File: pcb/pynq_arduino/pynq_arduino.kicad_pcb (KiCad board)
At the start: 4 copper layers, 48.5 x 52 mm, 3 parts, among them J1 Conn_02x11_Odd_Even, J2 Conn_01x15_Pin

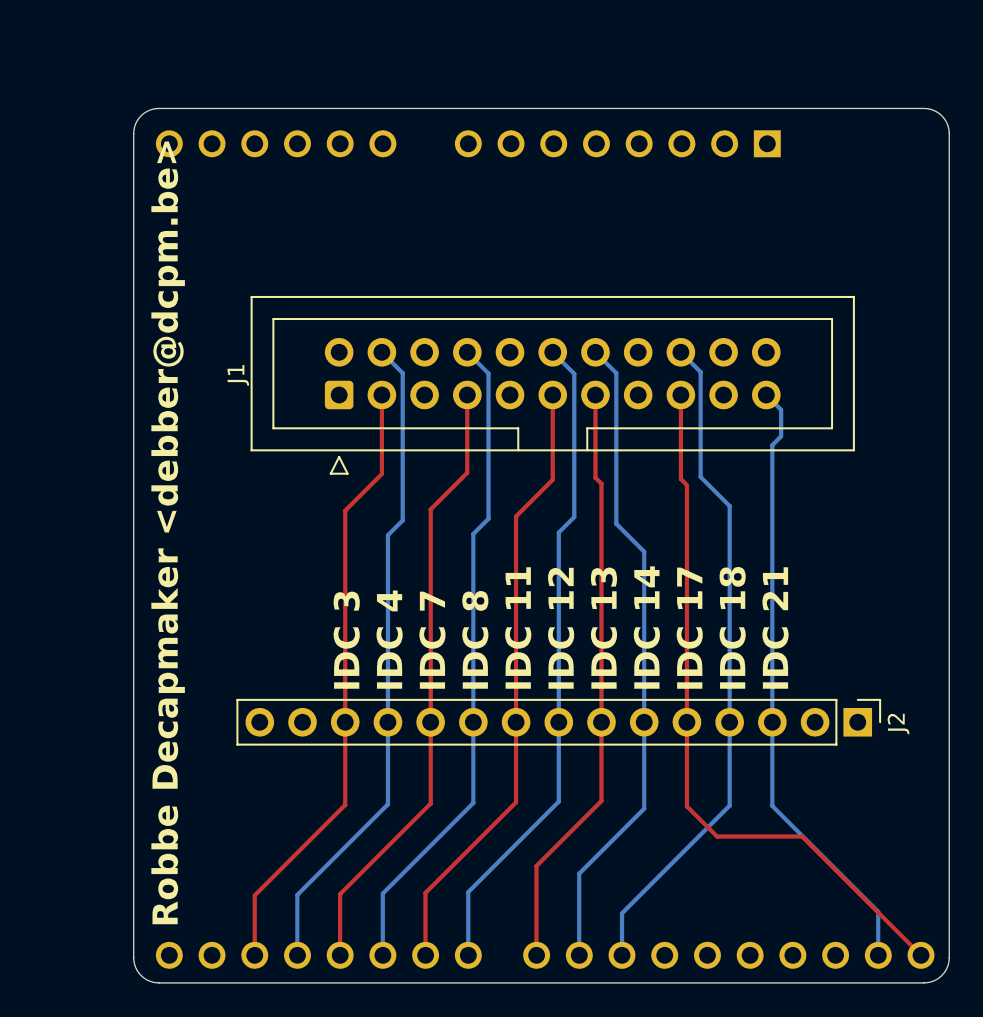
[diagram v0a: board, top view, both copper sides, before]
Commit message: Updating pynq pcb to have level shifters
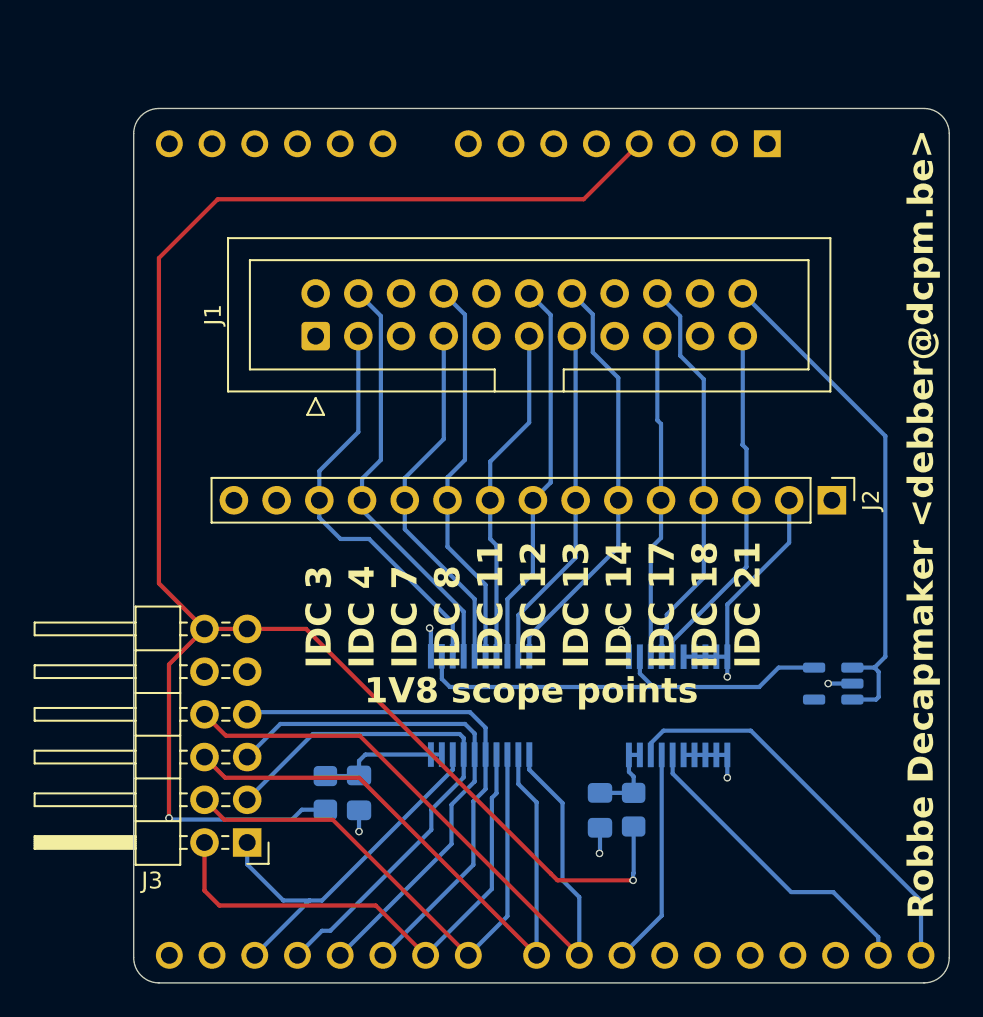
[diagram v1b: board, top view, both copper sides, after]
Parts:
- added C1: 0.1µF, Capacitor_SMD:C_0805_2012Metric_Pad1.18x1.45mm_HandSolder, B.Cu at (151.9, 94.2)
- added C2: 0.1µF, Capacitor_SMD:C_0805_2012Metric_Pad1.18x1.45mm_HandSolder, B.Cu at (166.2, 95.2)
- added J3: Conn_02x06_Odd_Even, Connector_PinHeader_2.54mm:PinHeader_2x06_P2.54mm_Horizontal, F.Cu at (145.2, 97.2)
- added R1: 200k, Resistor_SMD:R_0805_2012Metric_Pad1.20x1.40mm_HandSolder, B.Cu at (149.9, 94.2)
- added R2: 200k, Resistor_SMD:R_0805_2012Metric_Pad1.20x1.40mm_HandSolder, B.Cu at (168.2, 95.2)
- added U1: TPS7A0508PDBV, Package_TO_SOT_SMD:SOT-23-5, B.Cu at (180.1, 87.7)
- added U2: LSF0108QPWRQ1, level_shifter:PW20_TEX, B.Cu at (159.1, 89.0)
- added U3: LSF0108QPWRQ1, level_shifter:PW20_TEX, B.Cu at (170.9, 89.0)
- moved J2 13.3 mm to (180.0, 76.8)
- moved J1 3.77 mm to (149.3, 67.0)
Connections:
- A1 pad 17: IDC_1_3 -> IDC_1_3_a
- A1 pad 18: IDC_1_4 -> IDC_1_4_a
- A1 pad 19: IDC_1_7 -> IDC_1_7_a
- A1 pad 20: IDC_1_8 -> IDC_1_8_a
- A1 pad 21: IDC_1_11 -> IDC_1_11_a
- A1 pad 22: IDC_1_12 -> IDC_1_12_a
- A1 pad 23: IDC_1_13 -> IDC_1_13_a
- A1 pad 24: IDC_1_14 -> IDC_1_14_a
- A1 pad 25: IDC_1_18 -> IDC_1_18_a
- A1 pad 31: IDC_1_21 -> IDC_1_21_a
- A1 pad 32: IDC_1_17 -> IDC_1_17_a
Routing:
- net +3.3V: track 0.00 -> 111.1 mm, vias 0 -> 2
- net IDC_1_14_a: track 0.00 -> 41.4 mm
- net IDC_1_13_a: track 0.00 -> 37.0 mm
- net IDC_1_12_a: track 0.00 -> 32.4 mm
- net IDC_1_4_a: track 0.00 -> 31.9 mm
- net IDC_1_7_a: track 0.00 -> 31.4 mm
- net IDC_1_11_a: track 0.00 -> 31.3 mm
- net +5VD: track 0.00 -> 30.8 mm
- net IDC_1_8_a: track 0.00 -> 30.7 mm
- net GND: track 0.00 -> 26.3 mm, vias 0 -> 7
- net +1V8: track 0.00 -> 26.3 mm
- net IDC_1_17_a: track 0.00 -> 24.5 mm
- net IDC_1_3_a: track 0.00 -> 23.2 mm
- net IDC_1_17: track 42.2 -> 19.4 mm
- net IDC_1_21_a: track 0.00 -> 18.4 mm
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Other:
- board text added: "1V8 scope points"
